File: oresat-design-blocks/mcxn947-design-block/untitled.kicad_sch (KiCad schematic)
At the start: 12 parts, among them J10 Conn_02x20_Odd_Even, J2 USB_C_Receptacle_USB2.0_14P, J9 Conn_02x20_Odd_Even, U1 MCXN947VKLT

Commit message: finished initial layout and routing
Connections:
- net GND: now also J9.10 (Pin_10), J9.19 (Pin_19), J9.20 (Pin_20), J9.29 (Pin_29), J9.31 (Pin_31), J9.33 (Pin_33), J9.35 (Pin_35), J9.37 (Pin_37), J9.38 (Pin_38), J9.39 (Pin_39), J9.40 (Pin_40)
- net P0_23: now also J9.2 (Pin_2)
- net P1_0: now also J9.1 (Pin_1)
- net P1_1: now also J9.4 (Pin_4)
- net P1_12: now also J9.11 (Pin_11)
- net P1_13: now also J9.14 (Pin_14)
- net P1_14: now also J9.12 (Pin_12)
- net P1_15: now also J9.13 (Pin_13)
- net P1_2: now also J9.3 (Pin_3)
- net P1_3: now also J9.9 (Pin_9)
- net P1_4: now also J9.6 (Pin_6)
- net P1_5: now also J9.5 (Pin_5)
- net P1_6: now also J9.8 (Pin_8)
- net P1_7: now also J9.7 (Pin_7)
- net at J9.15 (Pin_15): now also U1.14 (P2_0)
- net at J9.16 (Pin_16): now also U1.15 (P2_1)
- net at J9.17 (Pin_17): now also U1.16 (P2_2)
- net at J9.18 (Pin_18): now also U1.17 (P2_3)
- net at J9.21 (Pin_21): now also U1.18 (P2_4)
- net at J9.22 (Pin_22): now also U1.22 (P4_0/ANA_0)
- net at J9.23 (Pin_23): now also U1.19 (P2_5)
- net at J9.24 (Pin_24): now also U1.23 (P4_1/ANA_1)
- net at J9.25 (Pin_25): now also U1.20 (P2_6)
- net at J9.26 (Pin_26): now also U1.24 (P4_2)
- net at J9.27 (Pin_27): now also U1.21 (P2_7)
- net at J9.28 (Pin_28): now also U1.25 (P4_3)
- net at J9.30 (Pin_30): now also U1.26 (P4_4/ANA_4)
- net at J9.32 (Pin_32): now also U1.27 (P4_5/ANA_5)
- net at J9.34 (Pin_34): now also U1.28 (P4_6/ANA_6)
- net at J9.36 (Pin_36): now also U1.29 (P4_7/ANA_7)
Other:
- note added: "TO DO: - add silkscreen labels for every breakout pin - Add any additional pins we want"
- note added: "free available pins"
- note removed: "add silkscreen labels for every breakout? might be nice."
- moved on the sheet: C1, J10, J2, J9, R1, R2, TP13, TP14, TP15, TP16, U1D, U1E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

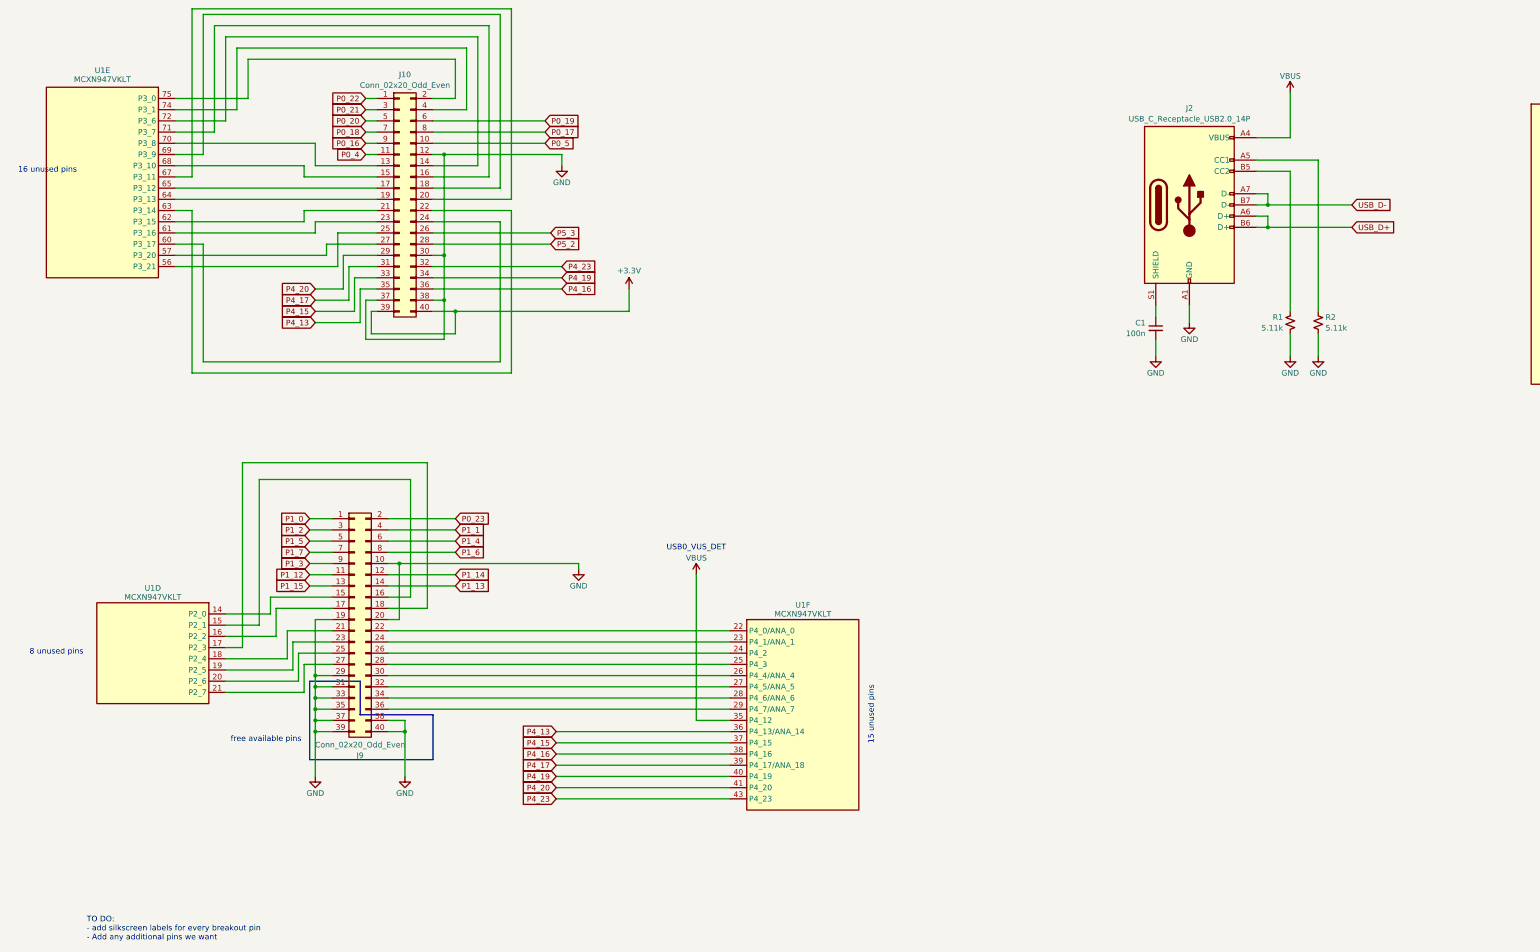
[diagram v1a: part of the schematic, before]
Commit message: Final revision after design review. Added labels for all breakout pins and cleaned up silkscreen.
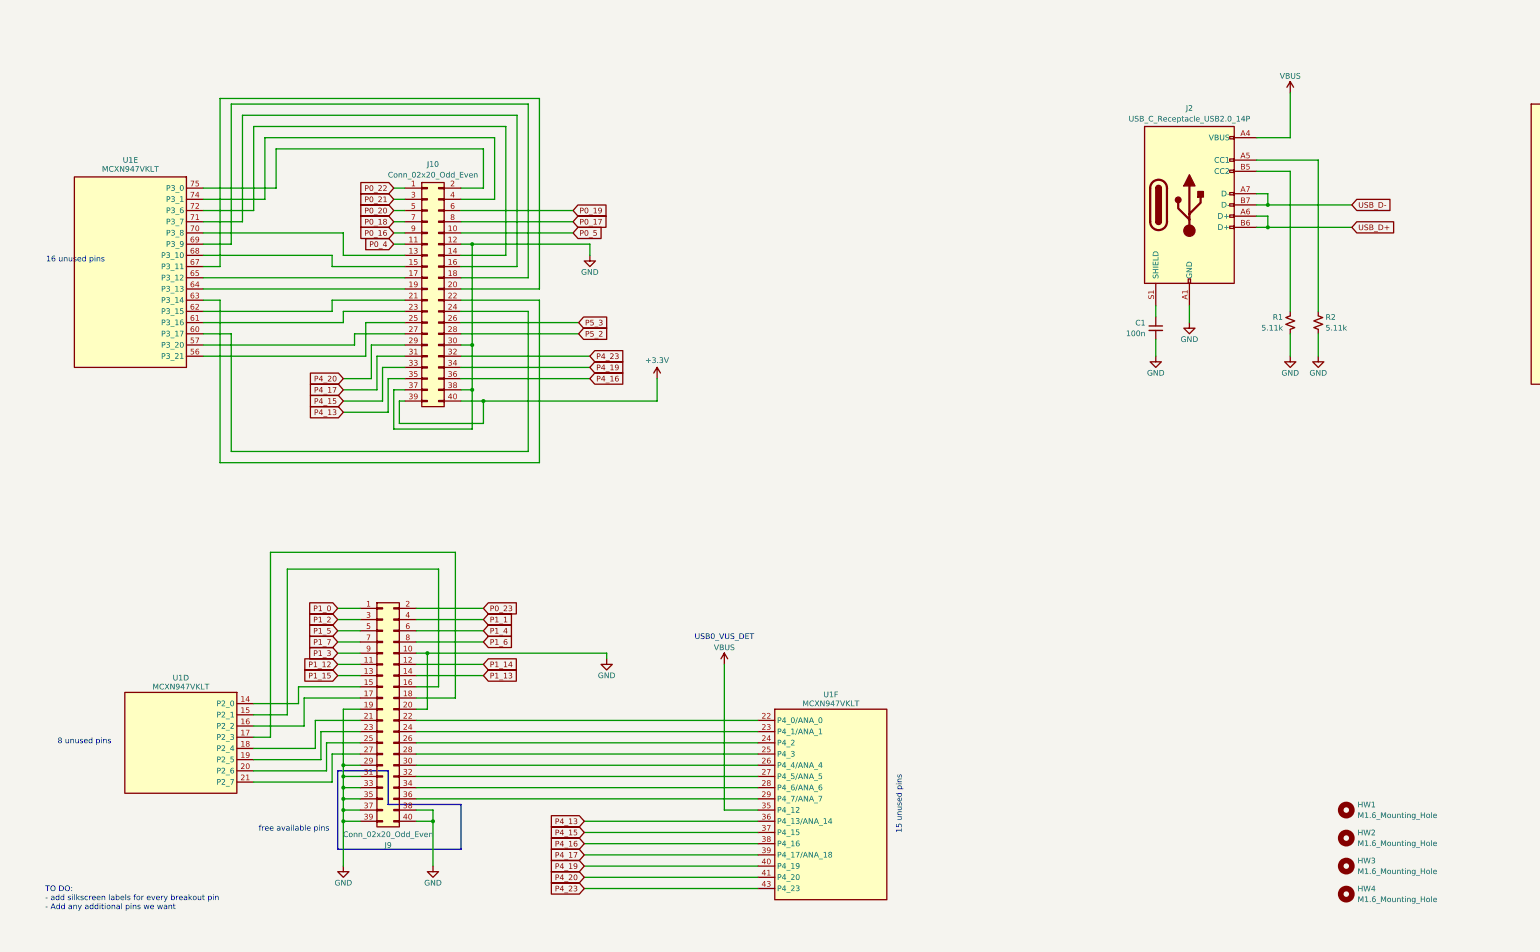
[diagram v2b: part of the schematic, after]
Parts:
- added HW1, HW2, HW3, HW4: M1.6_Mounting_Hole, oresat-misc:M1.6 Mounting Hole, symbol oresat-misc:M1.6_Mounting_Hole
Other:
- moved on the sheet: J10, J9, U1D, U1E, U1F

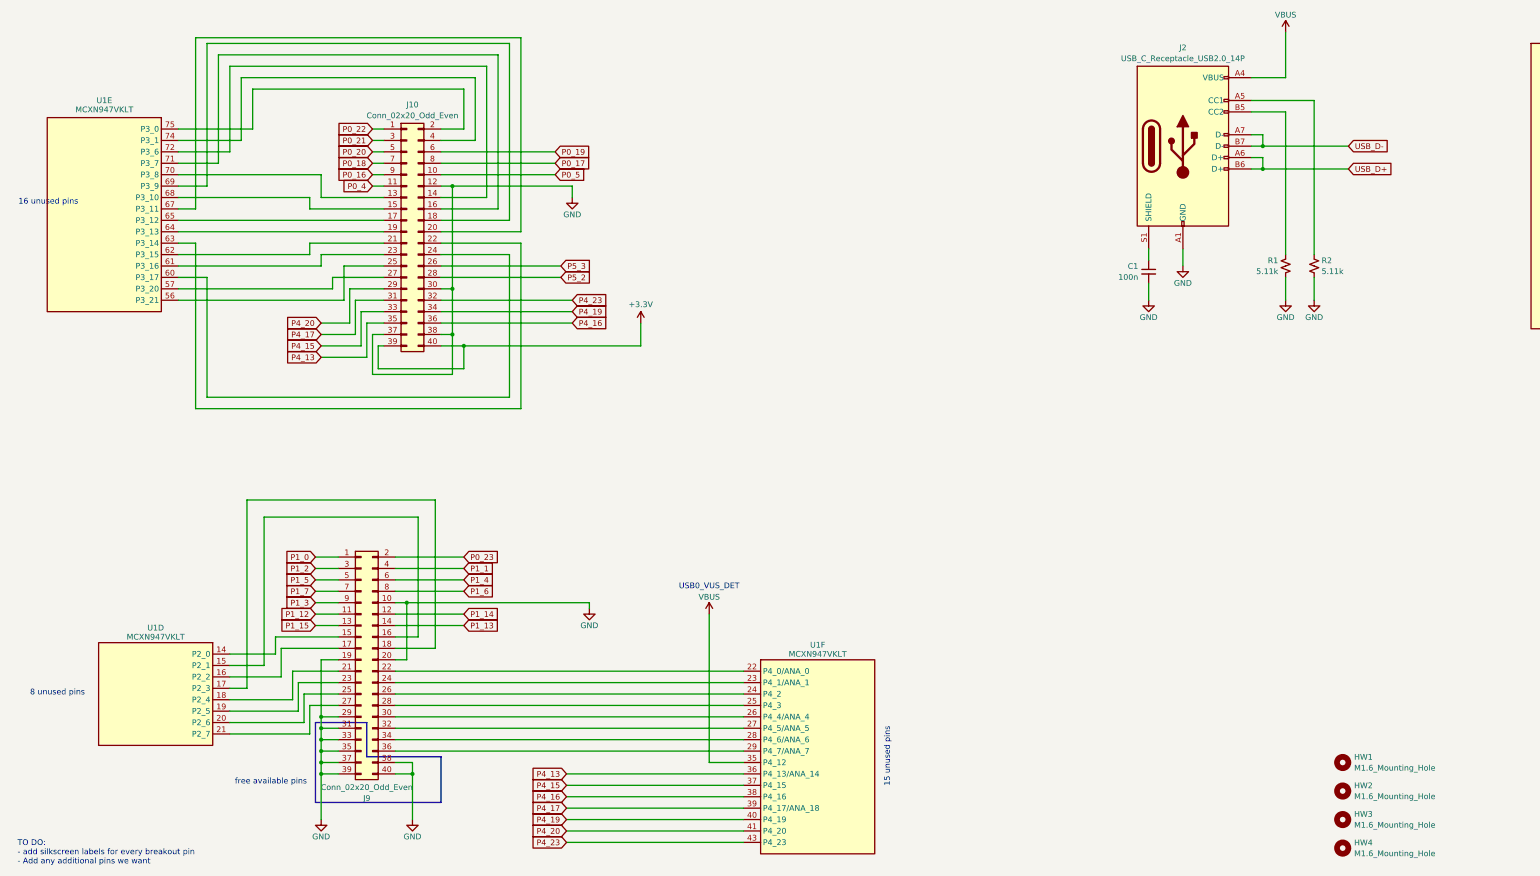
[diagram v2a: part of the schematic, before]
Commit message: Some ERC checking and fixing, and then dep dive into oresat passive library. Sorry Anna. Go fix all the silkscreen.
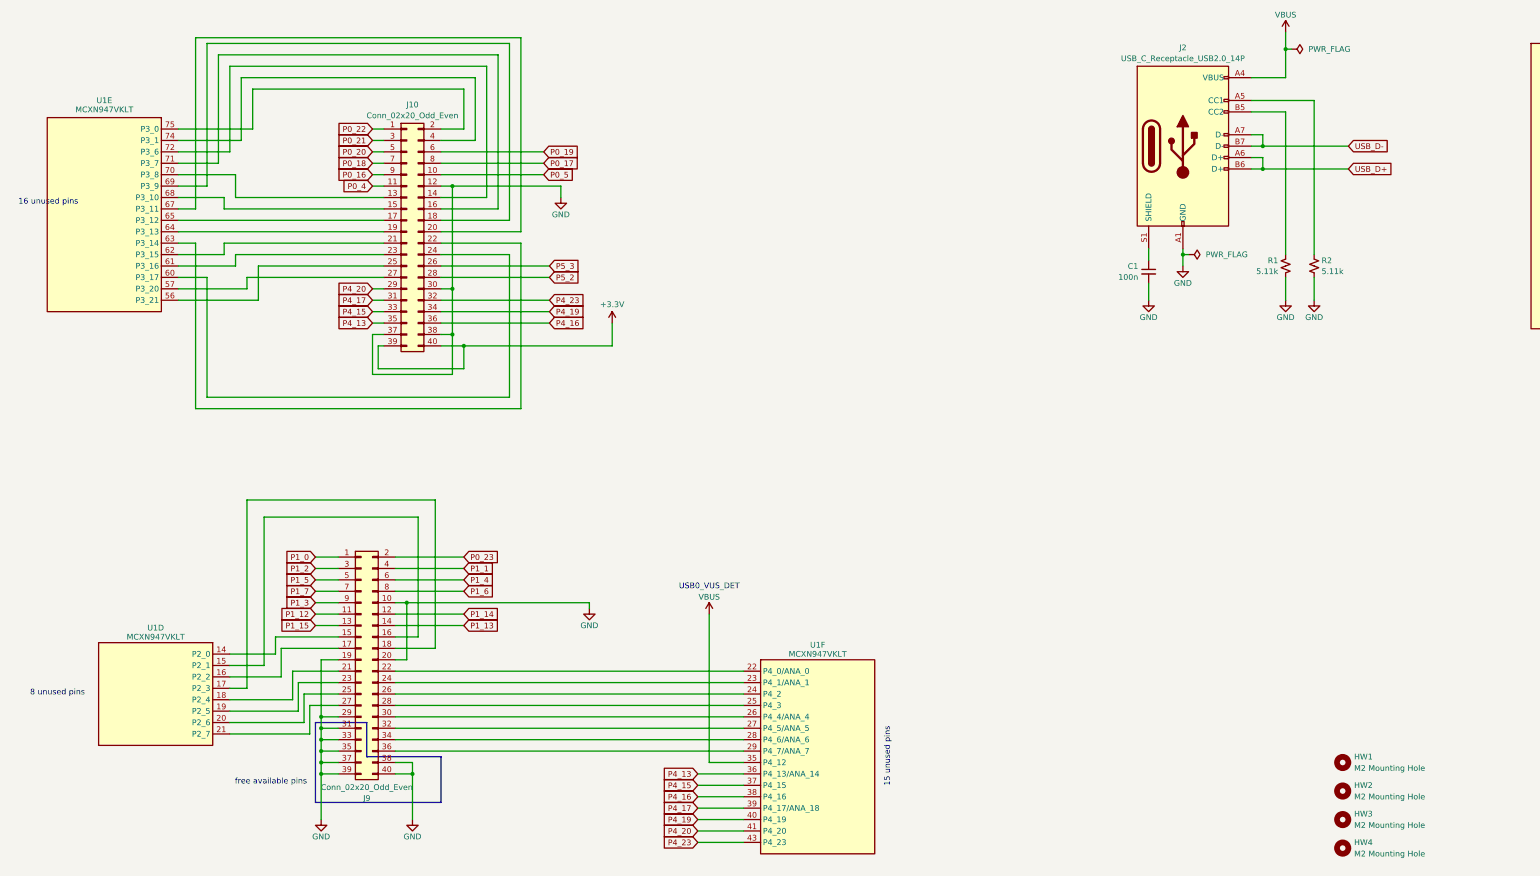
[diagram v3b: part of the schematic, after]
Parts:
- C1, R1, R2: footprint oresat-passives:0603-B-NOSILK -> oresat-passives:0603-C-NOSILK
- HW1, HW2, HW3, HW4: value M1.6_Mounting_Hole -> M2 Mounting Hole; footprint oresat-misc:M1.6 Mounting Hole -> oresat-misc:Hole-2.1mm-NPTH; symbol oresat-misc:M1.6_Mounting_Hole -> Mechanical:MountingHole
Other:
- note removed: "TO DO: - add silkscreen labels for every breakout pin - Add any additional pins we want"
